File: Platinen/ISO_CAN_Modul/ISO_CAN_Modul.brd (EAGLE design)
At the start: 35.1 x 27.9 mm, 26 parts, among them CON8 Term, IC1 MCP2515-I/P, IC2 ISO1050, IC3 B0505S-1W, X1 8 MHz, X2 Male, X3 Male, X4 Male, X5 AK500/2+M

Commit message: Logo & R1
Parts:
- flipped R1 to the bottom
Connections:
- net CAN_H: now also R1.2
- net GND2: no longer R1.2
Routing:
- net CAN_H: track 40.8 -> 52.0 mm
- net GND2: track 95.2 -> 86.3 mm
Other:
- board text added: "https://wiki.mobaledlib.de"
- board text removed: "https://wiki.mobaledlib.de/doku.php"

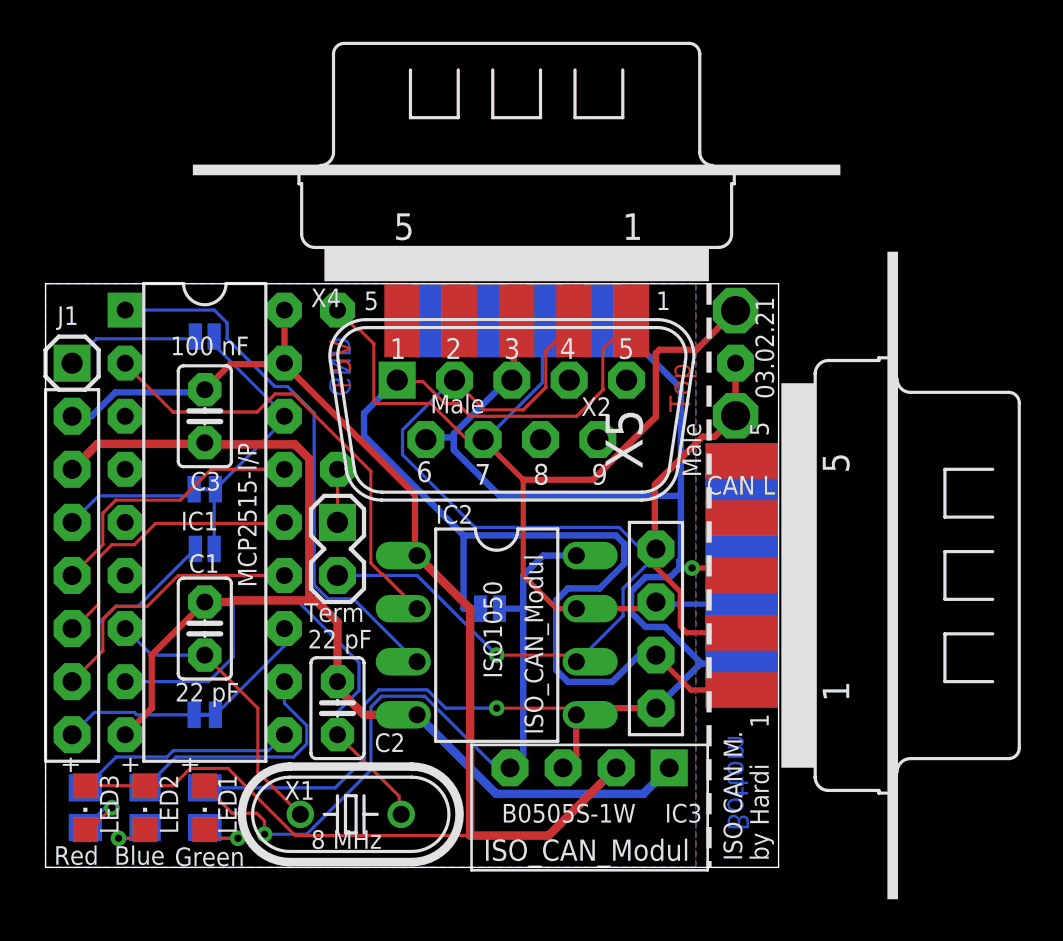
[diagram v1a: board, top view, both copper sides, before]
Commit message: Schaltplan - Netznamen ergänzt - Tippfehler korrigiert
Board
- SilkTop: Datum in sichtbaren Bereich verschoben
- Beschriftungen
	X5 verkleinert & verschoben, 
	IC1/MCP verschoben
	GREEN wie Red/Blue ausgerichtet
	Led1-3 ausgerichtet
	eine Beschriftung 'Male' weg (unter X5)
        und diverse andere Überlappungen behoben
	
- nachdem man X3 und X4 nicht falsch einbauen kann habe ich die Pin Beschriftungen 1 & 5 entfernt 
- Bauteilnamen R1-R3 passend zu Led1-Led3, Name von Led1 und Led3 vertauscht, ist am Board schöner
- Trennlinie auf der Oberseite entfernt, weil auch unten vorhanden. Damit ist mehr Platz für den Board Text
- Leiterbahnen verschoben für bessere RatsNest Abdeckung, zwei neue Durchkontaktierungen
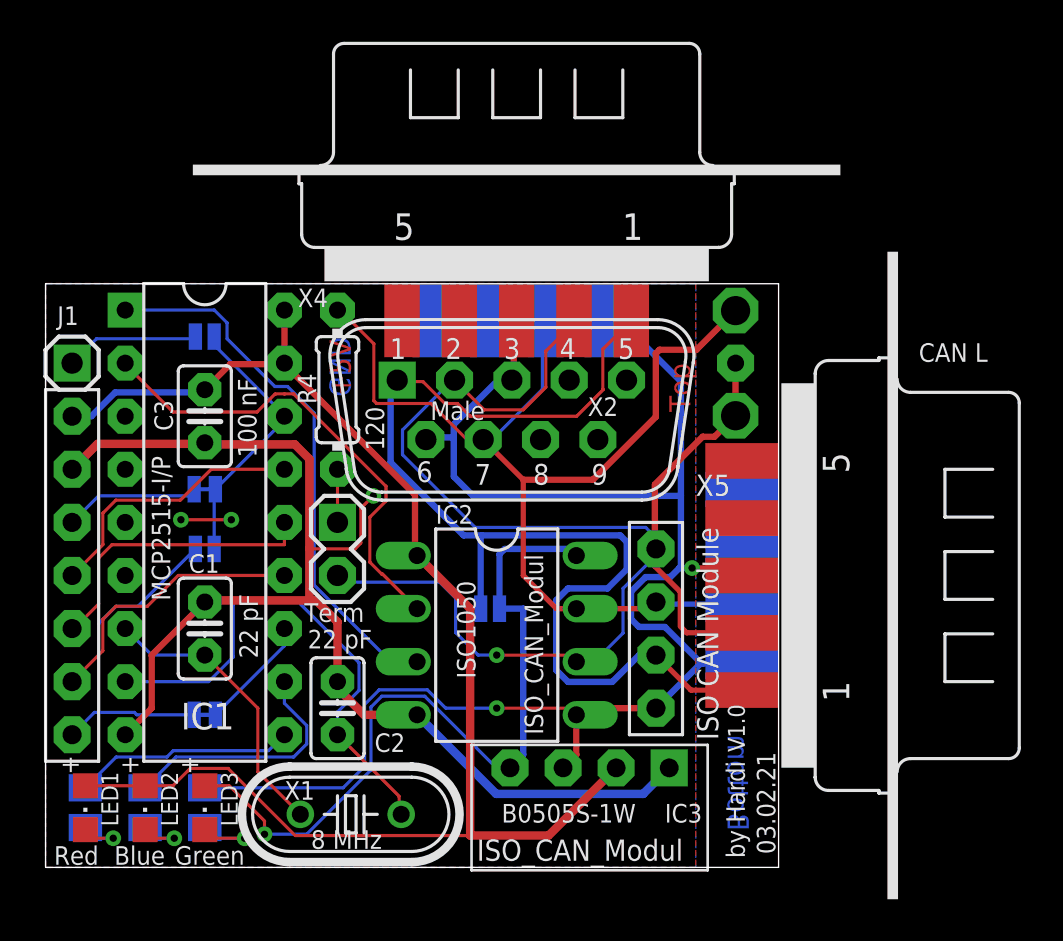
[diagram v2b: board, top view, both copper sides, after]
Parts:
- removed R11: 2K2, resistor:R0805
- removed R12: 1K, resistor:M0805
- added R3: 1K, resistor:M0805
- added R4: 120, resistor:0204/7
- LED1: value Green -> Red
- LED3: value Red -> Green
- R1: value 120 -> 1K; device resistor:0204/7 -> resistor:M0805
- R2: value 1K -> 2K2
- moved R1 23.4 mm to (1.91, 2.86)
- moved LED1 5.71 mm to (1.91, 2.86)
- moved LED3 5.71 mm to (7.62, 2.86)
- moved R2 2.86 mm to (4.76, 2.86), turned to 90 degrees
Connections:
- net N$1 renamed TXCAN
- net N$10 renamed CS_INT
- net N$11 renamed VCC2_EXT
- net N$2 renamed RXCAN
- net N$3 renamed OSC2
- net N$4 renamed OSC1
- net N$6 renamed CS_J1
- net N$8 renamed CS
- removed net N$12: CON8.1, R1.1
- removed net N$14: LED3.C, R12.1
- removed net N$5: LED1.C, R2.2
- removed net N$7: LED2.C, R11.1
- new net LED1: LED1.C, R1.1
- new net LED2: LED2.C, R2.1
- new net LED3: LED3.C, R3.2
- new net TERM: CON8.1, R4.1
- net +5V: now also LED1.A; no longer LED3.A
- net CAN_H: now also R4.2; no longer R1.2
- net GND2: now also R3.1; no longer R2.1
- net N$30: now also R1.2; no longer R12.2
- net N$9: now also R2.2; no longer R11.2
- net VCC2: now also LED3.A; no longer LED1.A
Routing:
- net GND: track 55.4 -> 62.9 mm, vias 0 -> 3
- net LED3: track 0.00 -> 4.19 mm, vias 0 -> 1
- net N$5: track 3.56 -> 0.00 mm, vias 1 -> 0
- net N$14: track 3.37 -> 0.00 mm, vias 1 -> 0
- net LED2: track 0.00 -> 3.18 mm, vias 0 -> 1
- net LED1: track 0.00 -> 3.05 mm, vias 0 -> 1
- net N$7: track 2.92 -> 0.00 mm, vias 1 -> 0
- net TERM: track 0.00 -> 2.54 mm
- net N$12: track 2.54 -> 0.00 mm
- net VCC2: track 35.4 -> 37.4 mm
- net CAN_L: track 66.3 -> 68.0 mm
- net GND2: track 86.3 -> 87.9 mm
- net VCC2_EXT: track 55.8 -> 54.4 mm
- net RXCAN: track 22.2 -> 22.8 mm
- net SI: track 13.6 -> 14.2 mm
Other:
- board text added: "ISO CAN Module"
- board text added: "V1.0"
- board text removed: "1"
- board text removed: "5"
- board text removed: "ISO CAN M."
